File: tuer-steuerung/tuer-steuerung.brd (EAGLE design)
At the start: 65.7 x 67.3 mm, 47 parts, among them IC1 L6203, IC2 MEGA8-P, Q1 16Mhz, T1 BC337, T2 BC337

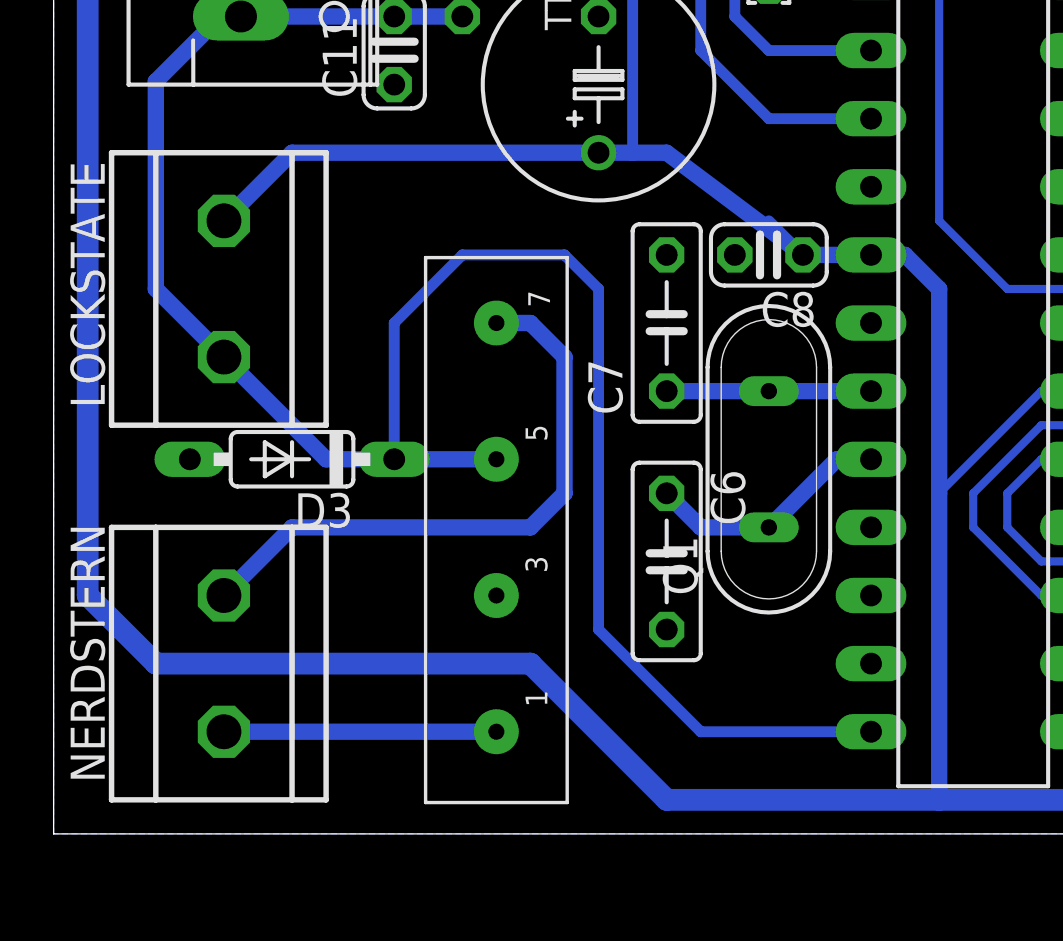
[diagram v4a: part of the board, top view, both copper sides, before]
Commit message: Quartz-Positionierung gemäß Application Note
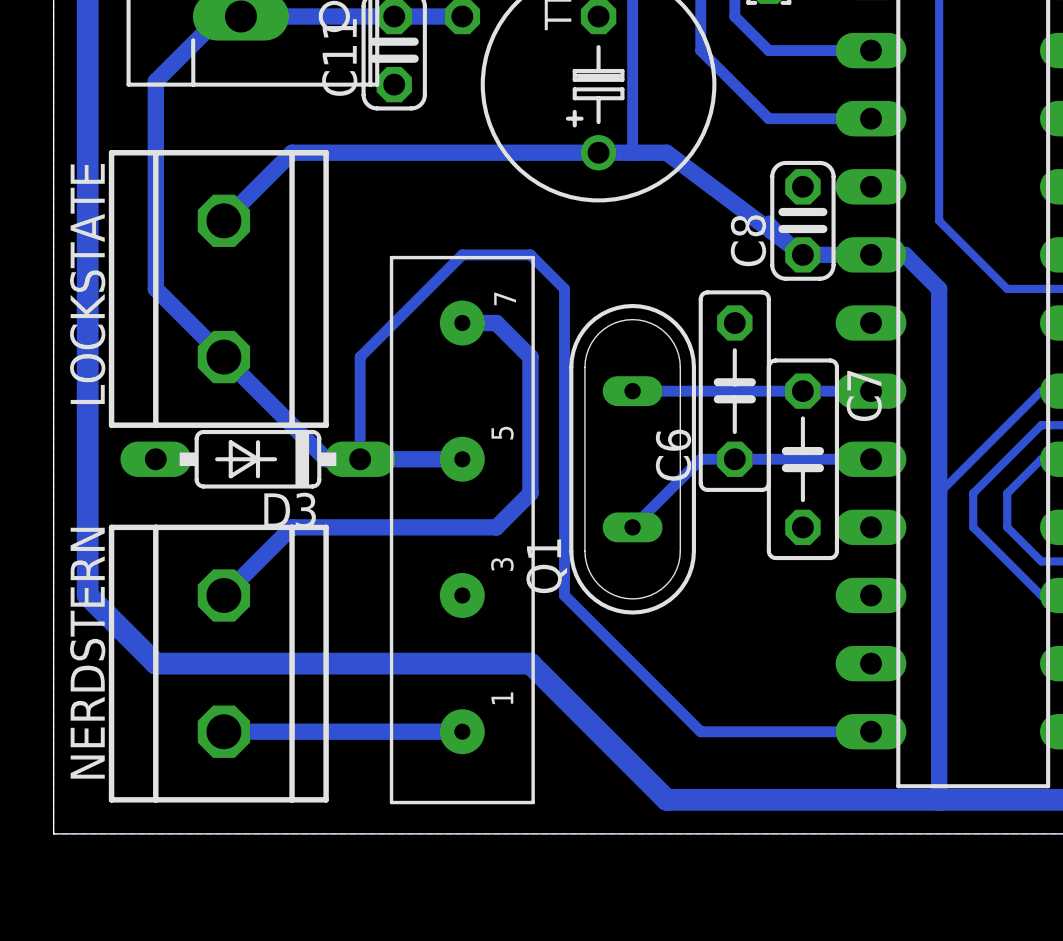
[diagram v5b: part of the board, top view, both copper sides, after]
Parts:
- moved C7 7.18 mm to (27.9, 14.0), turned to 270 degrees
- moved C6 6.84 mm to (25.4, 16.5), turned to 90 degrees
- moved Q1 5.08 mm to (21.6, 14.0)
- moved C8 1.80 mm to (27.9, 22.9), turned to 90 degrees
- moved U$2 1.27 mm to (15.2, 11.4)
- moved D3 1.27 mm to (7.62, 14.0)
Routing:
- net LOCKSTATE: track 74.2 -> 72.7 mm
- net N$5: track 10.2 -> 8.89 mm
- net N$2: track 7.62 -> 8.89 mm
- net N$4: track 22.4 -> 21.2 mm
- net N$1: track 9.20 -> 9.94 mm
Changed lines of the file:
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@@
 <attribute name="OC_FARNELL" value="unknown" x="-13.97" y="-11.43" size="1.778" layer="27" rot="R270" display="off"/>
 </element>
-<element name="Q1" library="special" package="QS" value="16Mhz" x="26.67" y="13.97" rot="R90"/>
+<element name="Q1" library="special" package="QS" value="16Mhz" x="21.59" y="13.97" rot="R90"/>
 <element name="D1" library="diode" package="DO35-7" value="" x="49.53" y="57.15" rot="R270"/>
 <element name="D2" library="diode" package="DO35-7" value="" x="52.07" y="59.69" rot="R270"/>
@@
 <element name="R5" library="resistor" package="0204/5" value="10K" x="50.8" y="30.48" rot="R270"/>
 <element name="R6" library="resistor" package="0204/5" value="10K" x="15.24" y="33.02" rot="R90"/>
-<element name="U$2" library="n39" package="SIL05-1A72" value="SIL05-1A72" x="16.51" y="11.43" rot="R90"/>
-<element name="D3" library="diode" package="DO35-7" value="" x="8.89" y="13.97" rot="R180"/>
+<element name="U$2" library="n39" package="SIL05-1A72" value="SIL05-1A72" x="15.24" y="11.43" rot="R90"/>
+<element name="D3" library="diode" package="DO35-7" value="" x="7.62" y="13.97" rot="R180"/>
 <element name="T1" library="transistor" package="TO92" value="BC337" x="49.53" y="10.16" rot="R90"/>
 <element name="T2" library="transistor" package="TO92" value="BC337" x="49.53" y="3.81" rot="R270"/>
@@
 <element name="R9" library="resistor" package="0207/2V" value="" x="53.34" y="11.43" rot="R90"/>
 <element name="R10" library="resistor" package="0207/2V" value="" x="53.34" y="3.81" rot="R90"/>
-<element name="C6" library="resistor" package="C050-025X075" value="12p" x="22.86" y="10.16" rot="R270"/>
-<element name="C7" library="resistor" package="C050-025X075" value="12p" x="22.86" y="19.05" rot="R90"/>
-<element name="C8" library="resistor" package="C025-024X044" value="100n" x="26.67" y="21.59" rot="R180"/>
+<element name="C6" library="resistor" package="C050-025X075" value="12p" x="25.4" y="16.51" rot="R90"/>
+<element name="C7" library="resistor" package="C050-025X075" value="12p" x="27.94" y="13.97" rot="R270"/>
+<element name="C8" library="resistor" package="C025-024X044" value="100n" x="27.94" y="22.86" rot="R90"/>
 <element name="C9" library="resistor" package="TAP5-80" value="470u" x="20.32" y="27.94" rot="R90"/>
 <element name="C10" library="resistor" package="TAP5-80" value="470u" x="21.59" y="48.26" rot="R180"/>
@@
 <contactref element="Q1" pad="1"/>
 <contactref element="C6" pad="1"/>
-<wire x1="26.67" y1="11.43" x2="29.21" y2="13.97" width="0.6096" layer="16"/>
-<wire x1="29.21" y1="13.97" x2="30.48" y2="13.97" width="0.6096" layer="16"/>
-<wire x1="22.86" y1="12.7" x2="24.13" y2="11.43" width="0.6096" layer="16"/>
-<wire x1="24.13" y1="11.43" x2="26.67" y2="11.43" width="0.6096" layer="16"/>
+<wire x1="21.59" y1="11.43" x2="24.13" y2="13.97" width="0.4064" layer="16"/>
+<wire x1="24.13" y1="13.97" x2="25.4" y2="13.97" width="0.4064" layer="16"/>
+<wire x1="25.4" y1="13.97" x2="30.48" y2="13.97" width="0.4064" layer="16"/>
 </signal>
 <signal name="N$2">
@@
 <contactref element="IC2" pad="9"/>
 <contactref element="C7" pad="1"/>
-<wire x1="30.48" y1="16.51" x2="26.67" y2="16.51" width="0.6096" layer="16"/>
-<wire x1="26.67" y1="16.51" x2="22.86" y2="16.51" width="0.6096" layer="16"/>
+<wire x1="21.59" y1="16.51" x2="27.94" y2="16.51" width="0.4064" layer="16"/>
+<wire x1="27.94" y1="16.51" x2="30.48" y2="16.51" width="0.4064" layer="16"/>
 </signal>
 <signal name="VDD">
@@
 <contactref element="U$2" pad="P5"/>
 <contactref element="D3" pad="C"/>
-<wire x1="16.51" y1="13.97" x2="12.7" y2="13.97" width="0.6096" layer="16"/>
+<wire x1="15.24" y1="13.97" x2="11.43" y2="13.97" width="0.6096" layer="16"/>
 <contactref element="HANDSHAKE" pad="4"/>
 <contactref element="C11" pad="2"/>
@@
 <wire x1="6.985" y1="30.48" x2="12.7" y2="30.48" width="0.6096" layer="16"/>
 <wire x1="3.81" y1="28.06" x2="3.81" y2="20.32" width="0.6096" layer="16"/>
-<wire x1="10.16" y1="13.97" x2="12.7" y2="13.97" width="0.6096" layer="16"/>
+<wire x1="10.16" y1="13.97" x2="11.43" y2="13.97" width="0.6096" layer="16"/>
 <contactref element="IC2" pad="14"/>
-<wire x1="12.7" y1="13.97" x2="12.7" y2="19.05" width="0.4064" layer="16"/>
-<wire x1="12.7" y1="19.05" x2="15.24" y2="21.59" width="0.4064" layer="16"/>
-<wire x1="15.24" y1="21.59" x2="19.05" y2="21.59" width="0.4064" layer="16"/>
-<wire x1="19.05" y1="21.59" x2="20.32" y2="20.32" width="0.4064" layer="16"/>
-<wire x1="20.32" y1="20.32" x2="20.32" y2="7.62" width="0.4064" layer="16"/>
-<wire x1="20.32" y1="7.62" x2="24.13" y2="3.81" width="0.4064" layer="16"/>
+<wire x1="11.43" y1="13.97" x2="11.43" y2="17.78" width="0.4064" layer="16"/>
+<wire x1="11.43" y1="17.78" x2="15.24" y2="21.59" width="0.4064" layer="16"/>
+<wire x1="15.24" y1="21.59" x2="17.78" y2="21.59" width="0.4064" layer="16"/>
+<wire x1="17.78" y1="21.59" x2="19.05" y2="20.32" width="0.4064" layer="16"/>
+<wire x1="19.05" y1="20.32" x2="19.05" y2="8.89" width="0.4064" layer="16"/>
+<wire x1="19.05" y1="8.89" x2="24.13" y2="3.81" width="0.4064" layer="16"/>
 <wire x1="24.13" y1="3.81" x2="30.48" y2="3.81" width="0.4064" layer="16"/>
 <wire x1="12.7" y1="30.48" x2="15.24" y2="30.48" width="0.6096" layer="16"/>
@@
 <signal name="N$4">
 <contactref element="U$2" pad="P7"/>
-<wire x1="17.78" y1="11.43" x2="19.05" y2="12.7" width="0.6096" layer="16"/>
-<wire x1="19.05" y1="12.7" x2="19.05" y2="17.78" width="0.6096" layer="16"/>
-<wire x1="19.05" y1="17.78" x2="17.78" y2="19.05" width="0.6096" layer="16"/>
-<wire x1="17.78" y1="19.05" x2="16.51" y2="19.05" width="0.6096" layer="16"/>
-<wire x1="8.89" y1="11.43" x2="17.78" y2="11.43" width="0.6096" layer="16"/>
+<wire x1="16.51" y1="11.43" x2="17.78" y2="12.7" width="0.6096" layer="16"/>
+<wire x1="17.78" y1="12.7" x2="17.78" y2="17.78" width="0.6096" layer="16"/>
+<wire x1="17.78" y1="17.78" x2="16.51" y2="19.05" width="0.6096" layer="16"/>
+<wire x1="16.51" y1="19.05" x2="15.24" y2="19.05" width="0.6096" layer="16"/>
+<wire x1="8.89" y1="11.43" x2="16.51" y2="11.43" width="0.6096" layer="16"/>
 <contactref element="NERDSTERN" pad="2"/>
 <wire x1="8.89" y1="11.43" x2="6.35" y2="8.89" width="0.6096" layer="16"/>
@@
 <contactref element="U$2" pad="P1"/>
 <contactref element="NERDSTERN" pad="1"/>
-<wire x1="6.35" y1="3.81" x2="16.51" y2="3.81" width="0.6096" layer="16"/>
+<wire x1="6.35" y1="3.81" x2="15.24" y2="3.81" width="0.6096" layer="16"/>
 </signal>
 <signal name="LED_G">

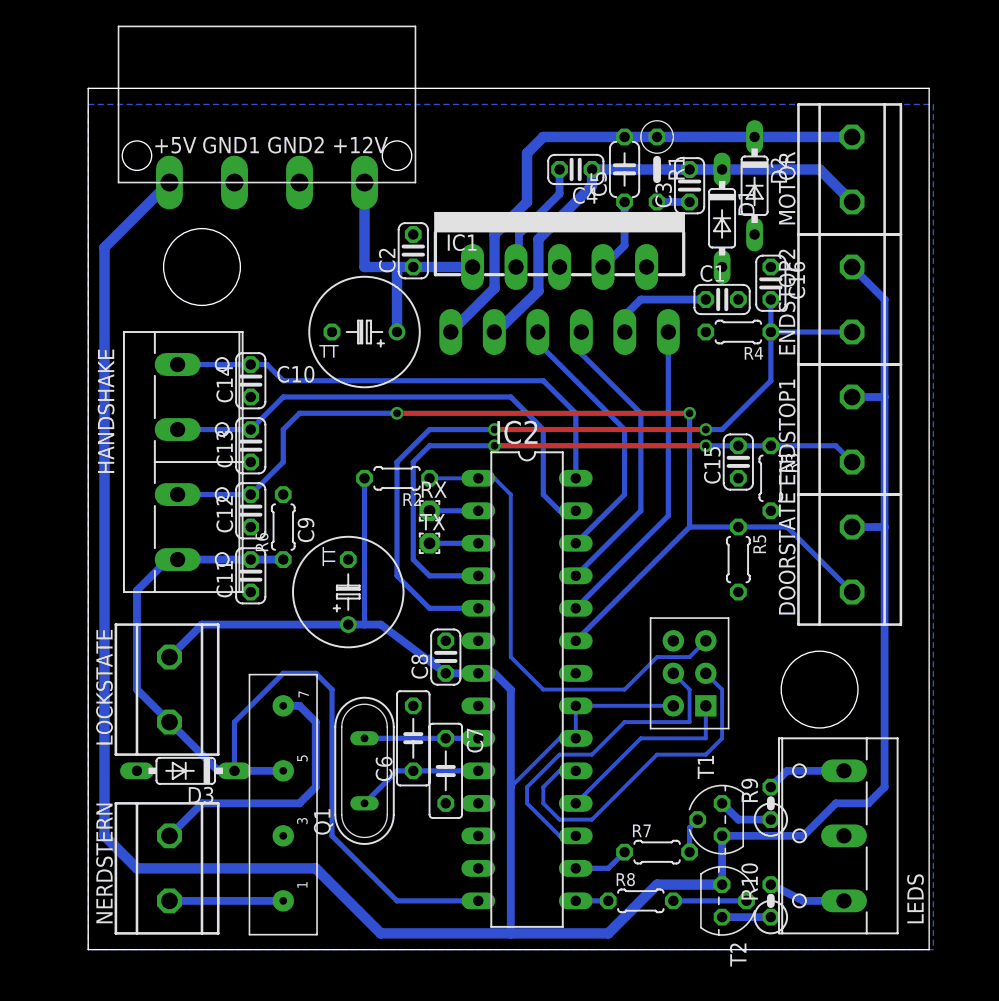
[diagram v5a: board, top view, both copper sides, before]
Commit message: Mindesgrößen der Pads und Vias angepasst
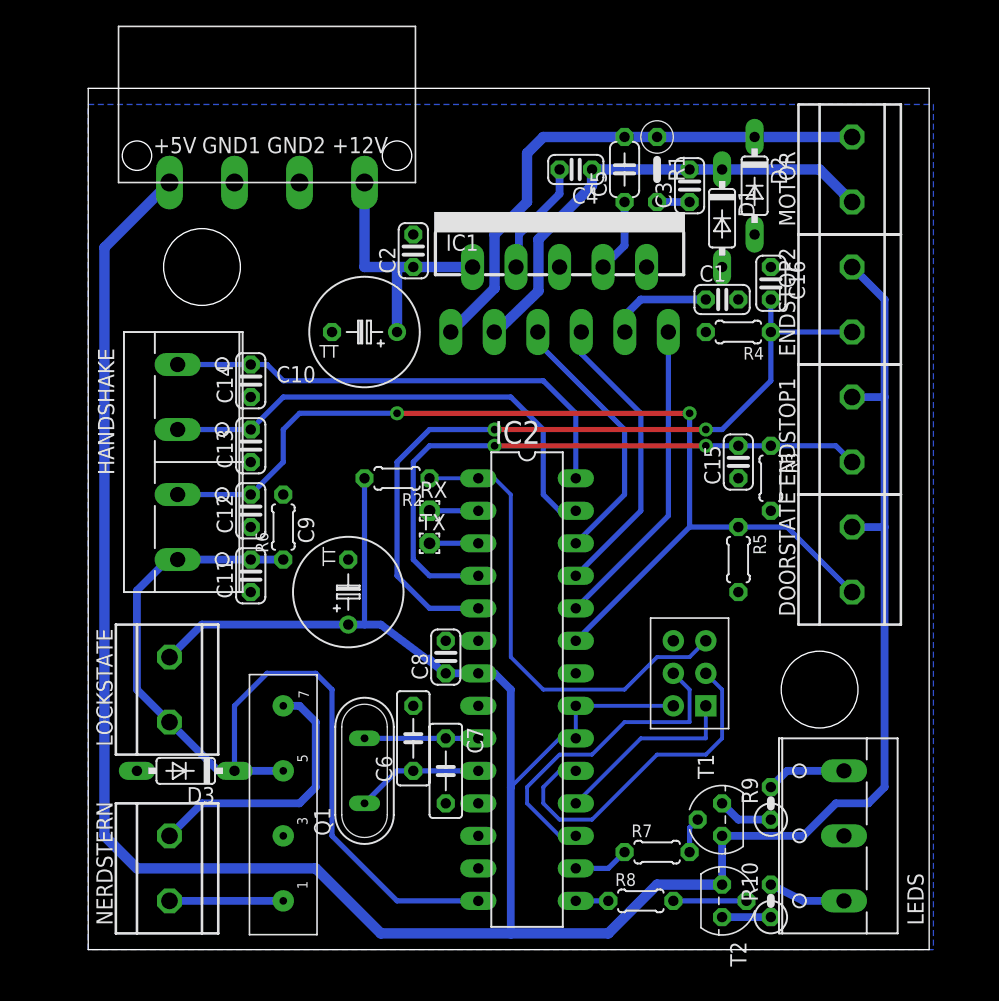
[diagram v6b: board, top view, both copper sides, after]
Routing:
- net LOCKSTATE: track 72.7 -> 73.5 mm
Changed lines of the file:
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@@
 </class>
 </classes>
-<designrules name="default">
+<designrules name="default *">
 <description language="de">&lt;b&gt;EAGLE Design Rules&lt;/b&gt;
 &lt;p&gt;
@@
 <param name="rvMicroViaOuter" value="0.25"/>
 <param name="rvMicroViaInner" value="0.25"/>
-<param name="rlMinPadTop" value="10mil"/>
+<param name="rlMinPadTop" value="12mil"/>
 <param name="rlMaxPadTop" value="20mil"/>
-<param name="rlMinPadInner" value="10mil"/>
+<param name="rlMinPadInner" value="12mil"/>
 <param name="rlMaxPadInner" value="20mil"/>
-<param name="rlMinPadBottom" value="10mil"/>
+<param name="rlMinPadBottom" value="12mil"/>
 <param name="rlMaxPadBottom" value="20mil"/>
-<param name="rlMinViaOuter" value="8mil"/>
+<param name="rlMinViaOuter" value="10mil"/>
 <param name="rlMaxViaOuter" value="20mil"/>
-<param name="rlMinViaInner" value="8mil"/>
+<param name="rlMinViaInner" value="10mil"/>
 <param name="rlMaxViaInner" value="20mil"/>
 <param name="rlMinMicroViaOuter" value="4mil"/>
@@
 <contactref element="C15" pad="2"/>
 <contactref element="IC2" pad="4"/>
-<via x="48.26" y="39.37" extent="1-16" drill="0.6" shape="square"/>
+<via x="48.26" y="39.37" extent="1-16" drill="0.6"/>
 <wire x1="48.26" y1="39.37" x2="31.75" y2="39.37" width="0.4064" layer="1"/>
-<via x="31.75" y="39.37" extent="1-16" drill="0.6" shape="square"/>
+<via x="31.75" y="39.37" extent="1-16" drill="0.6"/>
 <wire x1="48.26" y1="39.37" x2="50.8" y2="39.37" width="0.4064" layer="16"/>
 <wire x1="31.75" y1="39.37" x2="26.67" y2="39.37" width="0.4064" layer="16"/>
@@
 <contactref element="C16" pad="2"/>
 <contactref element="IC2" pad="5"/>
-<via x="48.26" y="40.64" extent="1-16" drill="0.6" shape="square"/>
+<via x="48.26" y="40.64" extent="1-16" drill="0.6"/>
 <wire x1="48.26" y1="40.64" x2="31.75" y2="40.64" width="0.4064" layer="1"/>
-<via x="31.75" y="40.64" extent="1-16" drill="0.6" shape="square"/>
+<via x="31.75" y="40.64" extent="1-16" drill="0.6"/>
 <wire x1="24.13" y1="38.1" x2="24.13" y2="29.21" width="0.4064" layer="16"/>
 <wire x1="24.13" y1="38.1" x2="26.67" y2="40.64" width="0.4064" layer="16"/>
@@
 <wire x1="10.16" y1="13.97" x2="11.43" y2="13.97" width="0.6096" layer="16"/>
 <contactref element="IC2" pad="14"/>
-<wire x1="11.43" y1="13.97" x2="11.43" y2="17.78" width="0.4064" layer="16"/>
-<wire x1="11.43" y1="17.78" x2="15.24" y2="21.59" width="0.4064" layer="16"/>
-<wire x1="15.24" y1="21.59" x2="17.78" y2="21.59" width="0.4064" layer="16"/>
+<wire x1="11.43" y1="13.97" x2="11.43" y2="19.05" width="0.4064" layer="16"/>
+<wire x1="11.43" y1="19.05" x2="13.97" y2="21.59" width="0.4064" layer="16"/>
+<wire x1="13.97" y1="21.59" x2="17.78" y2="21.59" width="0.4064" layer="16"/>
 <wire x1="17.78" y1="21.59" x2="19.05" y2="20.32" width="0.4064" layer="16"/>
 <wire x1="19.05" y1="20.32" x2="19.05" y2="8.89" width="0.4064" layer="16"/>

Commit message: SENSE -> GND
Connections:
- removed net M_SENSE: IC1.10
- net GND: now also IC1.10
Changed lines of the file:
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@@
 <param name="mdDrill" value="8mil"/>
 <param name="mdSmdStop" value="0mil"/>
-<param name="msWidth" value="10mil"/>
+<param name="msWidth" value="12mil"/>
 <param name="msDrill" value="24mil"/>
 <param name="msMicroVia" value="9.99mm"/>
@@
 </polygon>
 <contactref element="U$3" pad="GND"/>
+<contactref element="IC1" pad="10"/>
 </signal>
 <signal name="N$1">
@@
 <wire x1="41.91" y1="58.42" x2="41.91" y2="55.02" width="0.6096" layer="16"/>
 </signal>
-<signal name="M_SENSE">
-<contactref element="IC1" pad="10"/>
-</signal>
 <signal name="ENDSTOP1">
